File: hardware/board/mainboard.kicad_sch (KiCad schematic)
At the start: 0 parts

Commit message: Lots of various small changes after reviewing the checklist.
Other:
- note added: "4 Pole Diode Ladder Filter Designed By Carson Walls Inspired by Moritz Klein Simulations Link: https://github.com/wntrblm/Neptune/tree/main/simulation"
- note removed: "4 Pole Diode Ladder Filter Inspired by the filter by Moritz Klein"

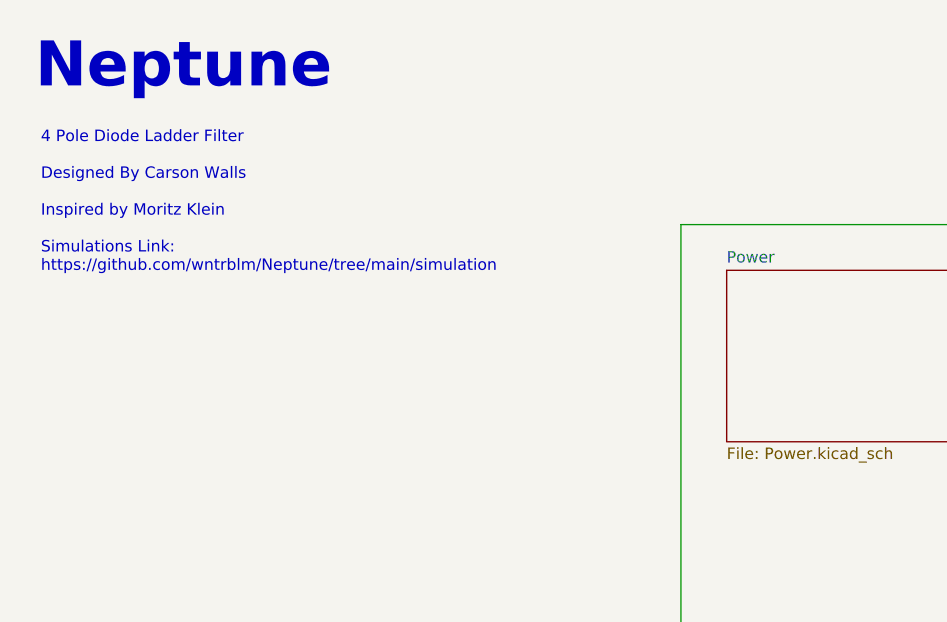
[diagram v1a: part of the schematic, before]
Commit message: hardware: update schematic fonts/text sizes, some slight readability improvements
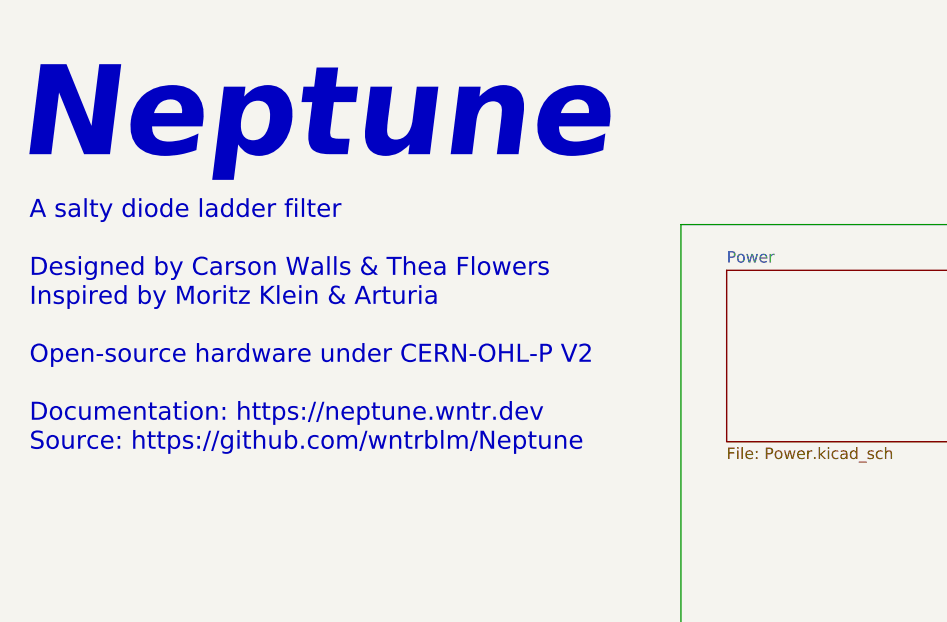
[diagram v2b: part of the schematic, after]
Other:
- note added: "A salty diode ladder filter Designed by Carson Walls & Thea Flowers Inspired by Moritz Klein & Arturia Open-source hardware under CERN-OHL-P V2 Documentation: https://neptune.wntr.dev Source: https://github.com/wntrblm/Neptune"
- note removed: "4 Pole Diode Ladder Filter Designed By Carson Walls Inspired by Moritz Klein Simulations Link: https://github.com/wntrblm/Neptune/tree/main/simulation"
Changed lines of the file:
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@@
   (title_block
     (title "Neptune")
-    (date "2023-10-10")
-    (rev "v1")
+    (date "2023-11-09")
+    (rev "v2")
     (company "Winterbloom")
     (comment 1 "Carson Walls")
@@
     (stroke (width 0) (type default))
   )
-  (text "Neptune" (at 17.78 25.4 0)
-    (effects (font (size 5 5) (thickness 0.508) bold) (justify left bottom))
+  (text "Neptune" (at 15.875 33.655 0)
+    (effects (font (face "Space Mono") (size 10 10) (thickness 0.508) bold italic) (justify left bottom))
   )
-  (text "4 Pole Diode Ladder Filter\n\nDesigned By Carson Walls\n\nInspired by Moritz Klein\n\nSimulations Link:\nhttps://github.com/wntrblm/Neptune/tree/main/simulation\n\n\n"
-    (at 18.415 49.53 0)
-    (effects (font (size 1.27 1.27)) (justify left bottom))
+  (text "A salty diode ladder filter\n\nDesigned by Carson Walls & Thea Flowers\nInspired by Moritz Klein & Arturia\n\nOpen-source hardware under CERN-OHL-P V2\n\nDocumentation: https://neptune.wntr.dev\nSource: https://github.com/wntrblm/Neptune"
+    (at 17.145 65.405 0)
+    (effects (font (face "Nunito") (size 2 2)) (justify left bottom))
   )
   (sheet (at 149.225 34.925) (size 38.1 15.24) (fields_autoplaced)

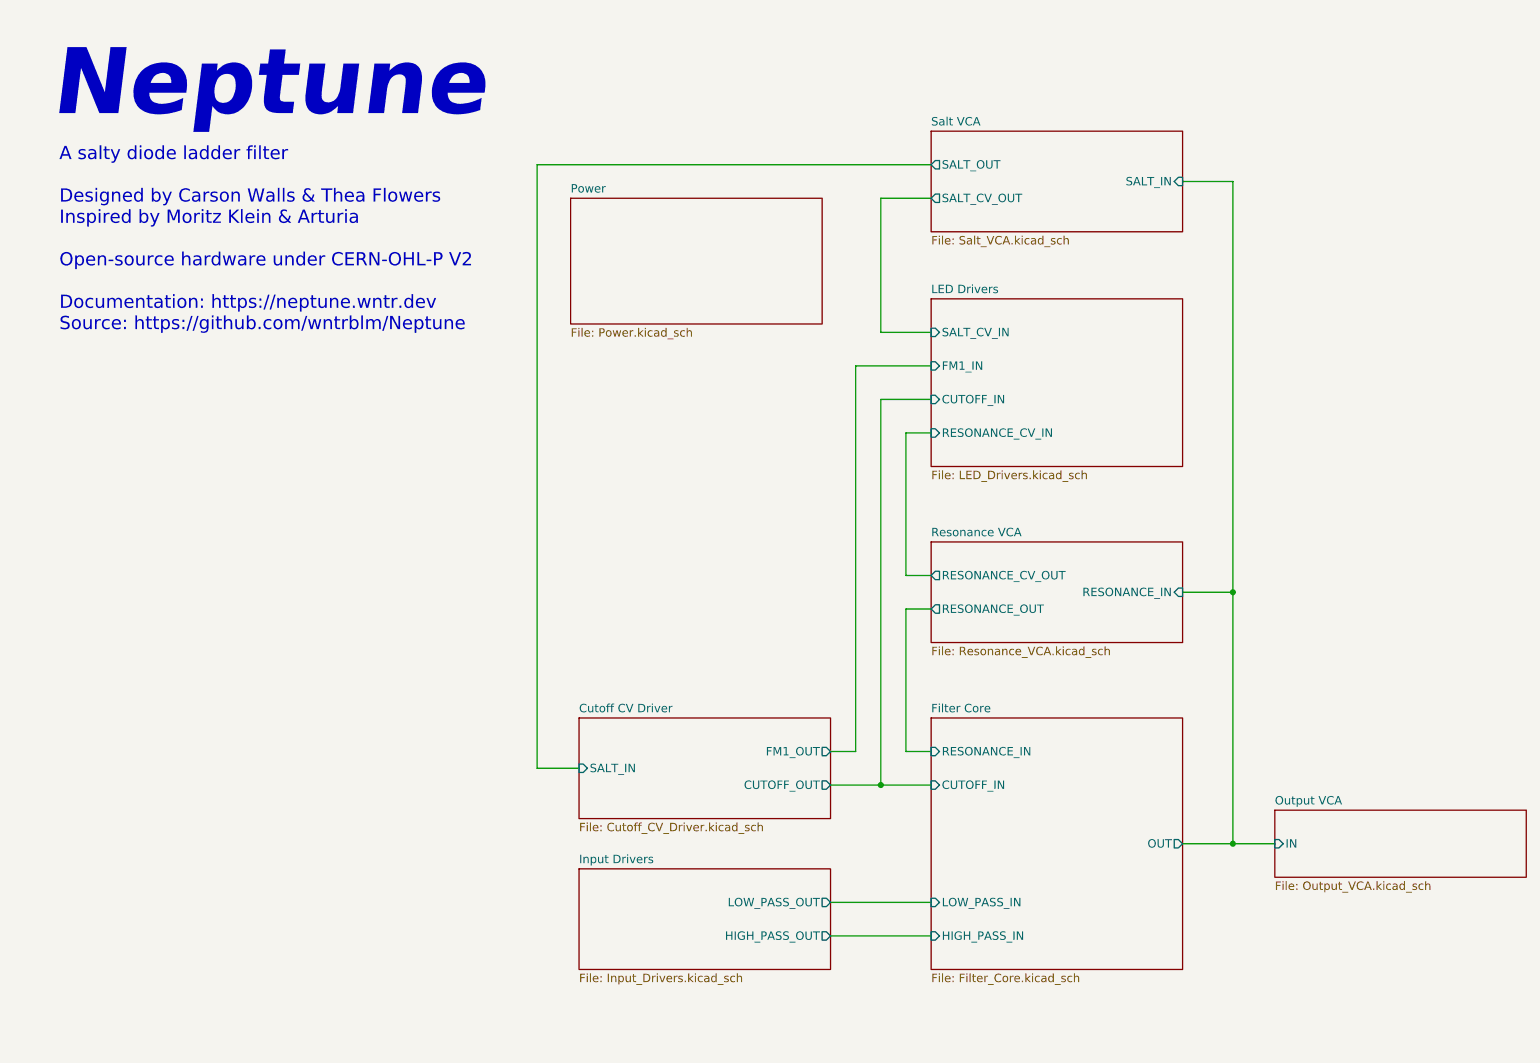
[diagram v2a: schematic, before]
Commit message: hardware: use new Winterbloom sheet layout
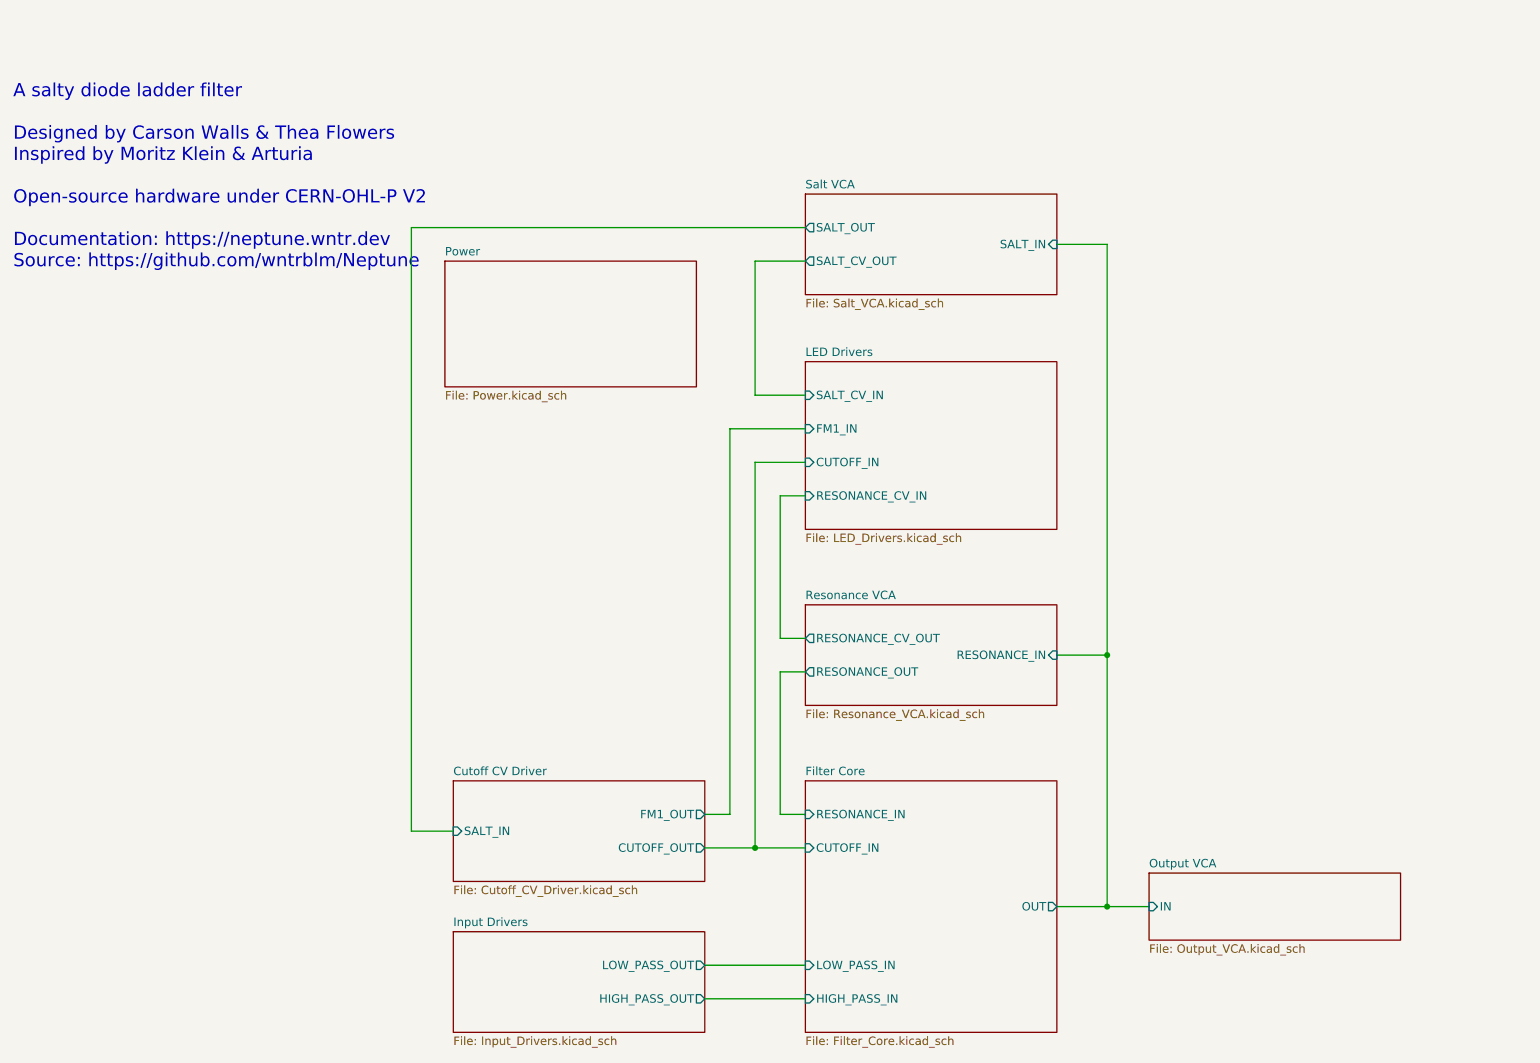
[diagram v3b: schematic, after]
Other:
- note removed: "Neptune"
